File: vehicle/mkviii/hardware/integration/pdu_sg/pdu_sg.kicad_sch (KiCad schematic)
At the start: 2 parts, among them U2 MCP23S17-E_SO, U3 STM32G441KBT6

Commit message: power
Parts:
- added C1, C2: C_0.1uF_50V, OEM:C_0603_1608Metric, symbol OEM:C_0.1uF_50V_0603
- added R1: R_100_0.1W, OEM:R_0603_1608Metric, symbol OEM:R_100_0.1W_0603
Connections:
- net +5V: now reaches U3.1 (VDD)
- net +5V: now also C1.1, R1.1
- net at U3.15 (VDDA): now also C2.1, R1.2
- new net GND: C1.2
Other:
- moved on the sheet: U3

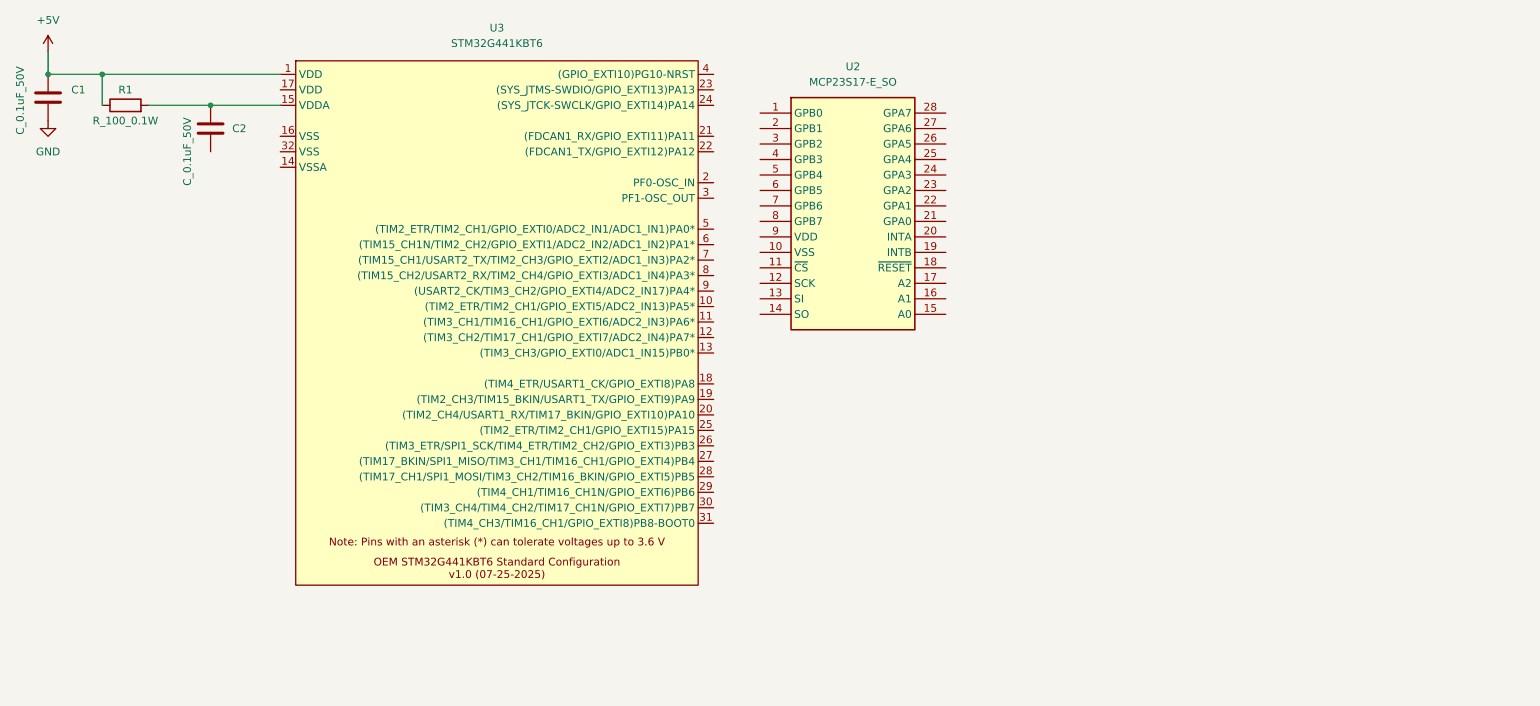
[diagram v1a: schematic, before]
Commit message: replicate general purpose stm32 mcu
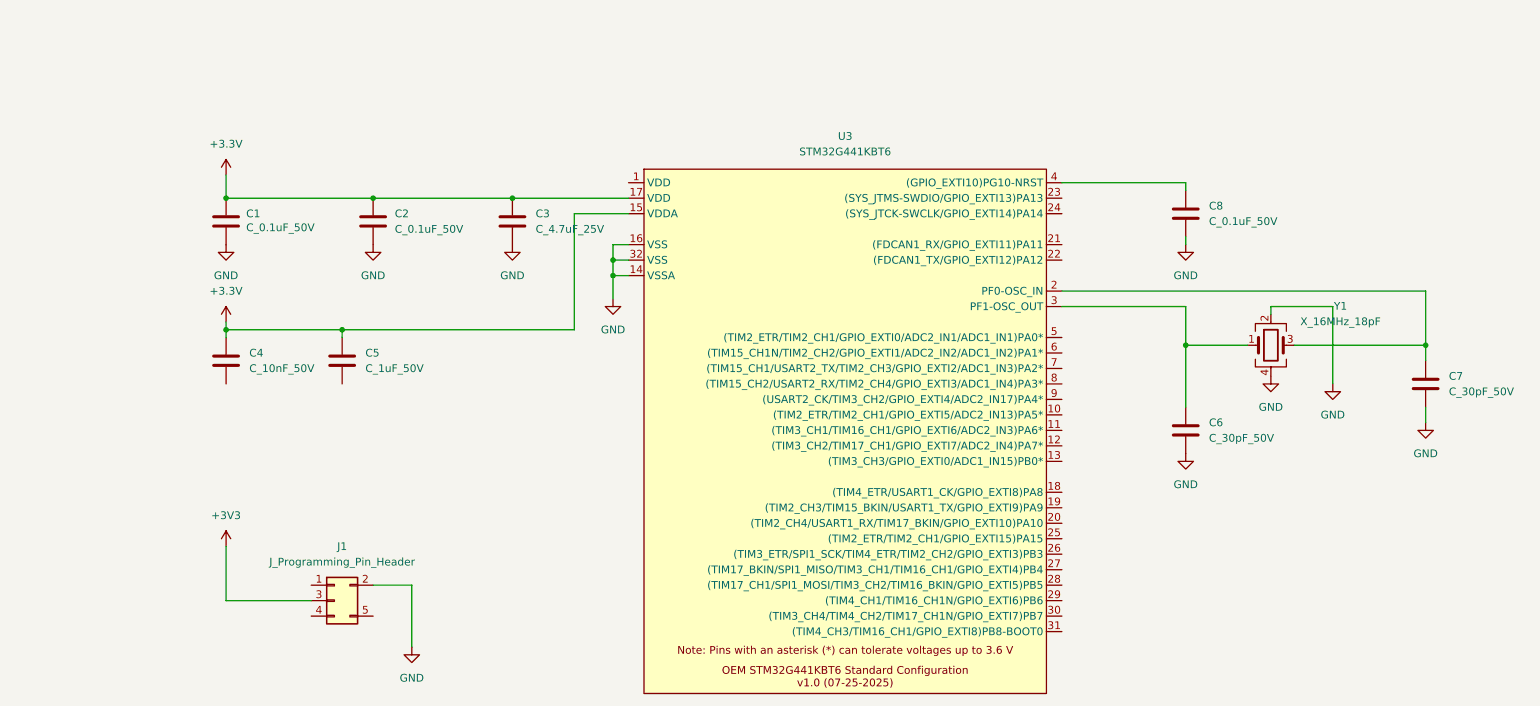
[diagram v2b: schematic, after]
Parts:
- removed R1: R_100_0.1W, OEM:R_0603_1608Metric, symbol OEM:R_100_0.1W_0603
- removed U2: MCP23S17-E_SO, OEM:U_SPI-IO-Xpndr_MCP23S17-E_SO_SOIC-28, symbol OEM:U_SPI-IO-Xpndr_MCP23S17-E_SO_SOIC-28
- added C3: C_4.7uF_25V, OEM:C_0603_1608Metric, symbol OEM:C_4.7uF_25V_0603
- added C4: C_10nF_50V, OEM:C_0603_1608Metric, symbol OEM:C_10nF_50V_0603
- added C5: C_1uF_50V, OEM:C_0603_1608Metric, symbol OEM:C_1uF_50V_0603
- added C6, C7: C_30pF_50V, OEM:C_0603_1608Metric, symbol OEM:C_30pF_50V_0603
- added C8: C_0.1uF_50V, OEM:C_0603_1608Metric, symbol OEM:C_0.1uF_50V_0603
- added J1: J_Programming_Pin_Header, stm32g441kbt6:Programming_Pin_Header_Keyed, symbol OEM:J_Programming_Pin_Header
- added Y1: X_16MHz_18pF, OEM:FA238160000MBC0 (X_16MHz_18pF_SMD - FA-238_16.0000MB-C0), symbol OEM:X_16MHz_18pF_SMD
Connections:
- net GND: now also C2.2, U3.14 (VSSA), U3.16 (VSS), U3.32 (VSS), C3.2, C6.2, C7.2, C8.2, J1.2 (Pin_2), Y1.2, Y1.4
- net +3.3V: now reaches C2.1, U3.15 (VDDA)
- net +3.3V: now also C1.1, U3.17 (VDD), C3.1, C4.1, C5.1
- net at U3.2 (PF0-OSC_IN): now also C7.1, Y1.3
- net at U3.3 (PF1-OSC_OUT): now also C6.1, Y1.1
- net at U3.4 ((GPIO_EXTI10)PG10-NRST): now also C8.1
- net +5V: no longer names the net of U3.1 (VDD)
- net +5V: no longer C1.1
- new net +3V3: J1.3 (Pin_3)
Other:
- moved on the sheet: C1, U3
